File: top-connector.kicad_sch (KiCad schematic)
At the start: 6 parts, among them J1 Compute-Module-4_Plug_Connect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, Q2 PJE138K

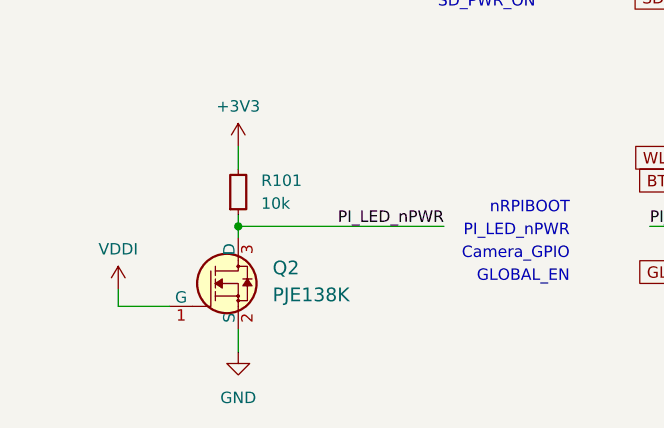
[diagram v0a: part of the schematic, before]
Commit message: [#59457] Optimize BOM
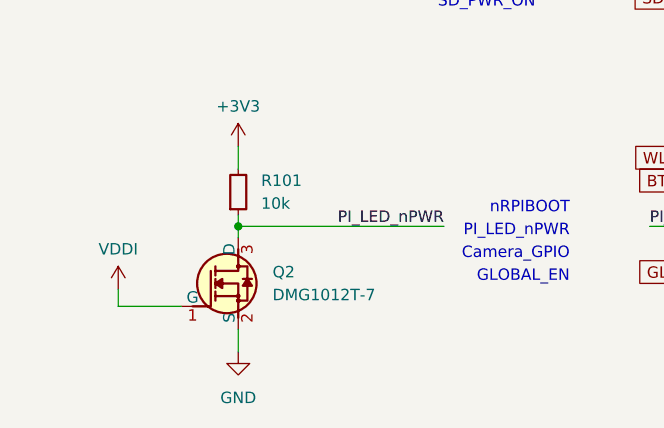
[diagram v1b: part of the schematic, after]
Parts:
- removed Q2: PJE138K, antmicro-footprints:SOT-523, symbol antmicroTransistorsFETsMOSFETsSingle:PJE138K
- added Q2: DMG1012T-7, antmicro-footprints:SOT-523, symbol antmicroTransistorsFETsMOSFETsSingle:DMG1012T-7
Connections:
- net GND: now also Q2.2 (S)
- net PI_LED_nPWR: now also Q2.3 (D)
- net VDDI: now also Q2.1 (G)
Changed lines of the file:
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@@
     (stroke (width 0) (type default))
   )
-  (wire (pts (xy 126.365 205.74) (xy 132.08 205.74))
+  (wire (pts (xy 126.365 205.74) (xy 133.35 205.74))
     (stroke (width 0) (type default))
   )
@@
         (path "/db4a0d3e-2eb3-499e-977d-6eb378cfd3ed/debae449-a92d-4184-817e-09f6daf3da7c"
           (reference "R1") (unit 1)
-        )
-      )
-    )
-  )
-  (symbol (lib_id "antmicroTransistorsFETsMOSFETsSingle:PJE138K") (at 132.08 205.74 0) (unit 1)
-    (in_bom yes) (on_board yes) (dnp no)
-    (property "Reference" "Q2" (at 143.51 201.4766 0)
-      (effects (font (size 1.524 1.524)) (justify left))
-    )
-    (property "Value" "PJE138K" (at 143.51 204.47 0)
-      (effects (font (size 1.524 1.524)) (justify left))
-    )
-    (property "Footprint" "antmicro-footprints:SOT-523" (at 137.16 200.66 0)
-      (effects (font (size 1.524 1.524)) (justify left) hide)
-    )
-    (property "Datasheet" "https://www.mouser.com/datasheet/2/1057/PJE138K-1876698.pdf" (at 137.16 198.12 0)
-      (effects (font (size 1.524 1.524)) (justify left) hide)
-    )
-    (property "MPN" "PJE138K_R1_00001" (at 148.59 195.58 0)
-      (effects (font (size 1.524 1.524)) (justify left) hide)
-    )
-    (property "Manufacturer" "PANJIT" (at 137.16 195.58 0)
-      (effects (font (size 1.524 1.524)) (justify left) hide)
-    )
-    (property "Author" "Antmicro" (at 154.94 227.33 0)
-      (effects (font (size 1.27 1.27) (thickness 0.15)) (justify left bottom) hide)
-    )
-    (property "License" "Apache-2.0" (at 154.94 229.87 0)
-      (effects (font (size 1.27 1.27) (thickness 0.15)) (justify left bottom) hide)
-    )
-    (pin "1")
-    (pin "2")
-    (pin "3")
-    (instances
-      (project "polarfire-som"
-        (path "/db4a0d3e-2eb3-499e-977d-6eb378cfd3ed/debae449-a92d-4184-817e-09f6daf3da7c"
-          (reference "Q2") (unit 1)
         )
       )
@@
         )
       )
+    )
+  )
+  (symbol (lib_id "antmicroTransistorsFETsMOSFETsSingle:DMG1012T-7") (at 133.35 205.74 0) (unit 1)
+    (in_bom yes) (on_board yes) (dnp no) (fields_autoplaced)
+    (property "Reference" "Q2" (at 143.51 201.93 0)
+      (effects (font (size 1.27 1.27) (thickness 0.15)) (justify left))
+    )
+    (property "Value" "DMG1012T-7" (at 143.51 209.55 0)
+      (effects (font (size 1.27 1.27) (thickness 0.15)) (justify left bottom) hide)
+    )
+    (property "Footprint" "antmicro-footprints:SOT-523" (at 143.51 212.09 0)
+      (effects (font (size 1.27 1.27) (thickness 0.15)) (justify left bottom) hide)
+    )
+    (property "Datasheet" "https://www.diodes.com/assets/Datasheets/ds31783.pdf" (at 143.51 214.63 0)
+      (effects (font (size 1.27 1.27) (thickness 0.15)) (justify left bottom) hide)
+    )
+    (property "MPN" "DMG1012T-7" (at 143.51 204.47 0)
+      (effects (font (size 1.27 1.27) (thickness 0.15)) (justify left))
+    )
+    (property "Manufacturer" "Diodes Incorporated" (at 143.51 207.01 0)
+      (effects (font (size 1.27 1.27) (thickness 0.15)) (justify left bottom) hide)
+    )
+    (property "Author" "Antmicro" (at 143.51 217.17 0)
+      (effects (font (size 1.27 1.27) (thickness 0.15)) (justify left bottom) hide)
+    )
+    (property "License" "Apache-2.0" (at 143.51 219.71 0)
+      (effects (font (size 1.27 1.27) (thickness 0.15)) (justify left bottom) hide)
+    )
+    (pin "1")
+    (pin "2")
+    (pin "3")
+    (instances
+      (project "polarfire-som"
+        (path "/db4a0d3e-2eb3-499e-977d-6eb378cfd3ed/debae449-a92d-4184-817e-09f6daf3da7c"
+          (reference "Q2") (unit 1)
+        )
+      )
